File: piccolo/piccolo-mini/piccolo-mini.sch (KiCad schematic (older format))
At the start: 18 parts, among them SW1 SW_Push, SW2 Rotary_Encoder_Switch, U1 ProMicro

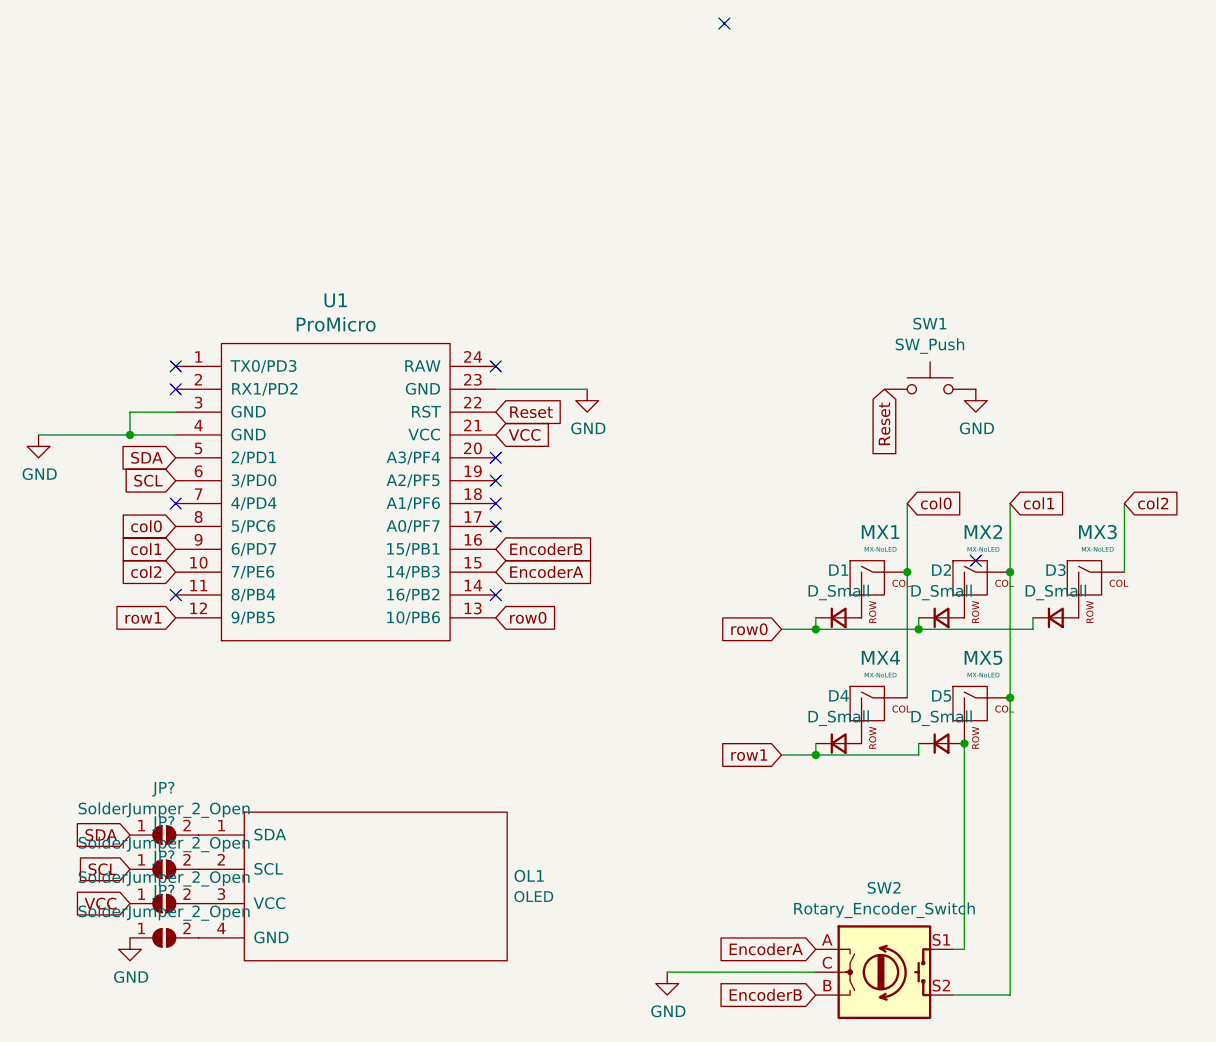
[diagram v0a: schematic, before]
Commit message: First prototype of piccolo ready for production
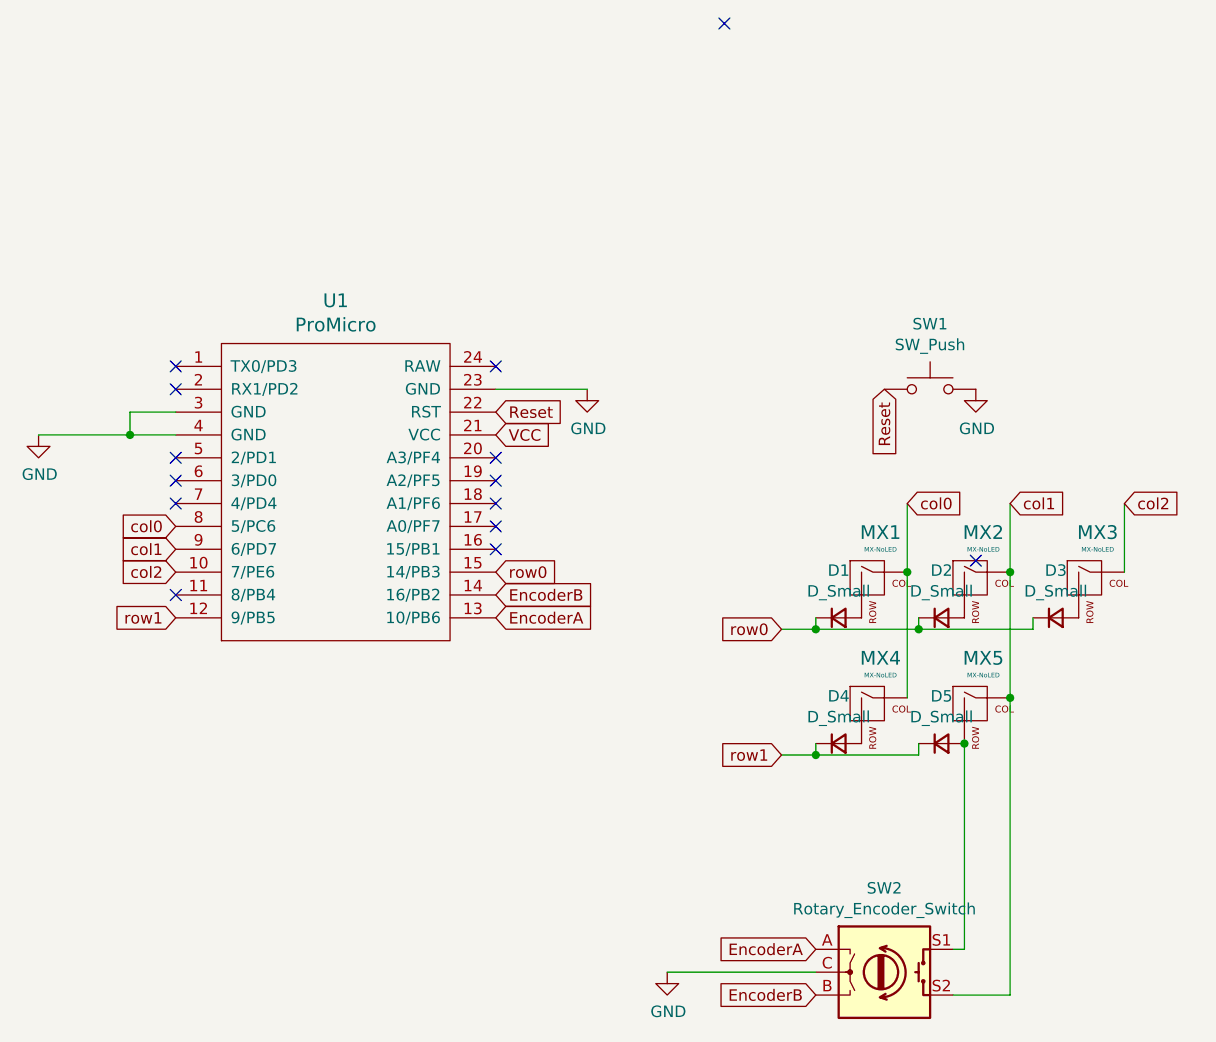
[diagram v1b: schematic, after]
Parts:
- removed JP? (x4): SolderJumper_2_Open, symbol Jumper:SolderJumper_2_Open
- removed OL1: OLED, kbd:OLED_v2, symbol kbd:OLED
- SW1: footprint Keebio-Parts:SW_Tactile_SPST_Angled_MJTP1117-no-mount -> kbd:ResetSW_1side
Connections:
- net EncoderA: now also U1.13 (10/PB6); no longer U1.15 (14/PB3)
- net EncoderB: now also U1.14 (16/PB2); no longer U1.16 (15/PB1)
- net row0: now also U1.15 (14/PB3); no longer U1.13 (10/PB6)
- net SCL: no longer names the net of U1.6 (3/PD0)
- net SDA: no longer names the net of U1.5 (2/PD1)
- no-connect marks 12 -> 14
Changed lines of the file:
@@
 F 0 "SW1" H 4950 2035 50  0000 C CNN
 F 1 "SW_Push" H 4950 1944 50  0000 C CNN
-F 2 "Keebio-Parts:SW_Tactile_SPST_Angled_MJTP1117-no-mount" H 4950 1950 50  0001 C CNN
+F 2 "kbd:ResetSW_1side" H 4950 1950 50  0001 C CNN
 F 3 "~" H 4950 1950 50  0001 C CNN
 	1    4950 1750
@@
 Text GLabel 4450 4400 0    50   Input ~ 0
 EncoderB
-Text GLabel 3050 2550 2    50   Input ~ 0
+Text GLabel 3050 2750 2    50   Input ~ 0
 EncoderA
-Text GLabel 3050 2450 2    50   Input ~ 0
+Text GLabel 3050 2650 2    50   Input ~ 0
 EncoderB
 $Comp
@@
 Wire Wire Line
 	4450 4300 3800 4300
-$Comp
-L kbd:OLED OL1
-U 1 1 61513CC3
-P 2500 3950
-F 0 "OL1" H 3128 4019 51  0000 L CNN
-F 1 "OLED" H 3128 3929 47  0000 L CNN
-F 2 "kbd:OLED_v2" H 2500 4050 60  0001 C CNN
-F 3 "" H 2500 4050 60  0001 C CNN
-	1    2500 3950
-	1    0    0    -1
-$EndComp
-Text GLabel 1450 3700 0    50   Input ~ 0
-SDA
-Text GLabel 1450 3850 0    50   Input ~ 0
-SCL
-Text GLabel 1450 4000 0    50   Input ~ 0
-VCC
-Text GLabel 1650 2050 0    50   Input ~ 0
-SDA
-Text GLabel 1650 2150 0    50   Input ~ 0
-SCL
-NoConn ~ 3050 2650
+NoConn ~ 3050 2450
 NoConn ~ 3050 2350
 NoConn ~ 3050 2250
@@
 	5300 4400 5300 3100
 Connection ~ 5300 3100
-Text GLabel 3050 2750 2    50   Input ~ 0
+Text GLabel 3050 2550 2    50   Input ~ 0
 row0
 NoConn ~ 1650 2650
-$Comp
-L Jumper:SolderJumper_2_Open JP?
-U 1 1 61578C34
-P 1600 3700
-F 0 "JP?" H 1600 3905 50  0000 C CNN
-F 1 "SolderJumper_2_Open" H 1600 3814 50  0000 C CNN
-F 2 "" H 1600 3700 50  0001 C CNN
-F 3 "~" H 1600 3700 50  0001 C CNN
-	1    1600 3700
-	1    0    0    -1
-$EndComp
-$Comp
-L Jumper:SolderJumper_2_Open JP?
-U 1 1 6157A6D9
-P 1600 3850
-F 0 "JP?" H 1600 4055 50  0000 C CNN
-F 1 "SolderJumper_2_Open" H 1600 3964 50  0000 C CNN
-F 2 "" H 1600 3850 50  0001 C CNN
-F 3 "~" H 1600 3850 50  0001 C CNN
-	1    1600 3850
-	1    0    0    -1
-$EndComp
-$Comp
-L Jumper:SolderJumper_2_Open JP?
-U 1 1 6157AD43
-P 1600 4000
-F 0 "JP?" H 1600 4205 50  0000 C CNN
-F 1 "SolderJumper_2_Open" H 1600 4114 50  0000 C CNN
-F 2 "" H 1600 4000 50  0001 C CNN
-F 3 "~" H 1600 4000 50  0001 C CNN
-	1    1600 4000
-	1    0    0    -1
-$EndComp
-$Comp
-L Jumper:SolderJumper_2_Open JP?
-U 1 1 6157B160
-P 1600 4150
-F 0 "JP?" H 1600 4355 50  0000 C CNN
-F 1 "SolderJumper_2_Open" H 1600 4264 50  0000 C CNN
-F 2 "" H 1600 4150 50  0001 C CNN
-F 3 "~" H 1600 4150 50  0001 C CNN
-	1    1600 4150
-	1    0    0    -1
-$EndComp
-$Comp
-L power:GND #PWR?
-U 1 1 6157FD67
-P 1450 4150
-F 0 "#PWR?" H 1450 3900 50  0001 C CNN
-F 1 "GND" H 1455 3977 50  0000 C CNN
-F 2 "" H 1450 4150 50  0001 C CNN
-F 3 "" H 1450 4150 50  0001 C CNN
-	1    1450 4150
-	1    0    0    -1
-$EndComp
+NoConn ~ 1650 2150
+NoConn ~ 1650 2050
 $EndSCHEMATC
